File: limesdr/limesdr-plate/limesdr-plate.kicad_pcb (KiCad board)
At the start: 2 copper layers, 106 x 55 mm, 20 parts

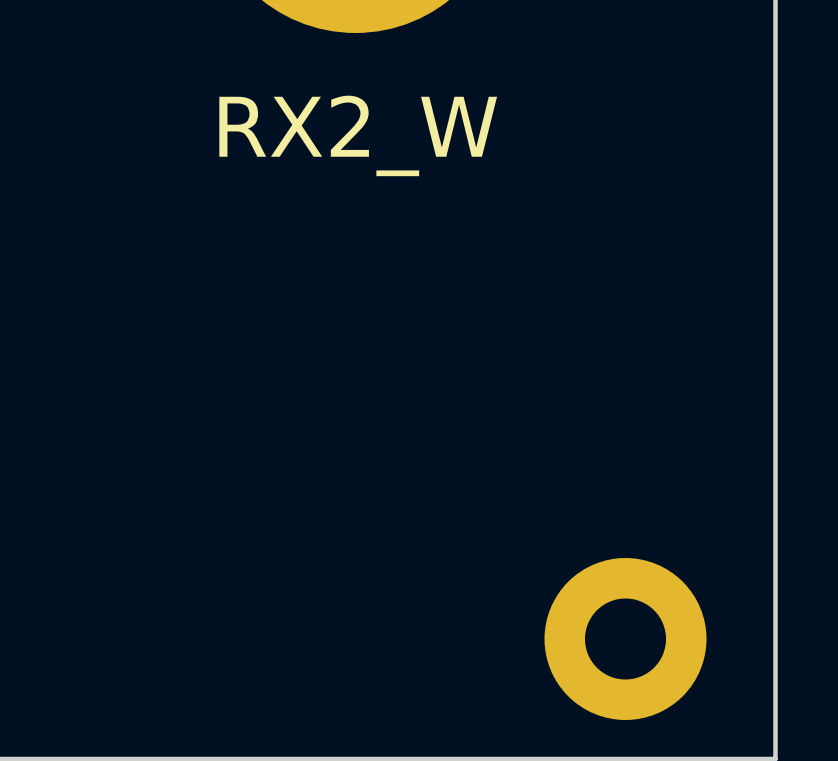
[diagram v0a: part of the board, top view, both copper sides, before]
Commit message: add leds
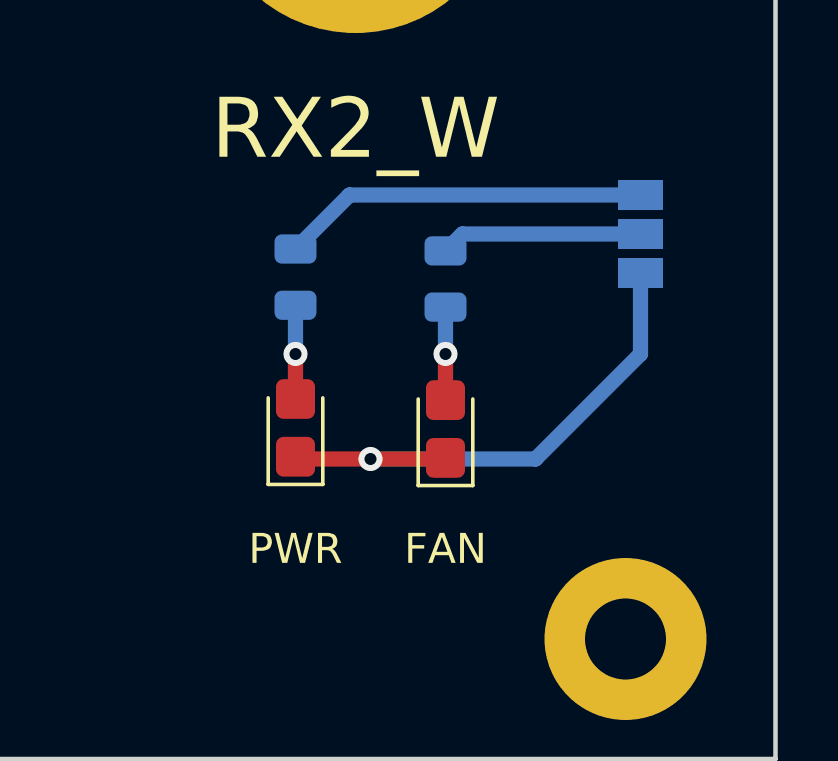
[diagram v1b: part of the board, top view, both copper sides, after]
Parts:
- added FAN: LED, Diode_SMD:D_0805_2012Metric_Castellated, F.Cu at (160.0, 60.0)
- added J1: Conn_01x03_Male, Jumper:SolderJumper-3_P1.3mm_Open_Pad1.0x1.5mm, B.Cu at (166.5, 53.5)
- added PWR: LED, Diode_SMD:D_0805_2012Metric_Castellated, F.Cu at (155.0, 60.0)
- added R1: R, Resistor_SMD:R_0805_2012Metric, B.Cu at (155.0, 54.9)
- added R2: R, Resistor_SMD:R_0805_2012Metric, B.Cu at (160.0, 55.0)
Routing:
- net GND: track 0.00 -> 18.2 mm, vias 0 -> 1
- net (no net): track 0.00 -> 12.2 mm
- net Net-(J1-Pad2): track 0.00 -> 6.73 mm
- net Net-(D1-Pad2): track 0.00 -> 3.12 mm, vias 0 -> 1
- net Net-(D2-Pad2): track 0.00 -> 3.10 mm, vias 0 -> 1
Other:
- board text added: "FAN"
- board text added: "GND"
- board text added: "JLCJLCJLCJLC"
- board text added: "PWR"
